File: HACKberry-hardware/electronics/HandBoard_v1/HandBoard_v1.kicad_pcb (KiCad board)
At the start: 2 copper layers, 60.8 x 54.8 mm, 10 parts, among them CON1 BARREL_JACK_MJ179PH, SW1 SW_PUSH_SKRGAQD010, SW2 SW_PUSH_SKRGAQD010, SW3 SW_PUSH_SKRGAQD010, SW4 SWITCH_SS-12SDP2, U2 3-CONDUCTOR_MINIATUIRE_JACK_M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, U3 Arduino_Micro, U5 Servo_Motor_MG90S, U6 Servo_Motor_S03N, U7 Servo_Motor_MG90S

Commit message: made the garber data of the HandBoard_v1
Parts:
- removed SW1, SW2, SW3: SW_PUSH_SKRGAQD010, HACKberry_v1:SKRGAQ0010
- removed SW4: SWITCH_SS-12SDP2, Pin_Headers:Pin_Header_Straight_1x03
- removed U7: Servo_Motor_MG90S, Pin_Headers:Pin_Header_Straight_1x03
- added SW1:MAX1: SW_PUSH_SKRGAQD010, HACKberry_v1:SKRGAQ0010, F.Cu at (101.5, 118.5)
- added SW2:MIN1: SW_PUSH_SKRGAQD010, HACKberry_v1:SKRGAQ0010, F.Cu at (113.0, 118.5)
- added SW3:Thumb1: SW_PUSH_SKRGAQD010, HACKberry_v1:SKRGAQ0010, F.Cu at (124.3, 118.5)
- added SW4:Middle1: SW_PUSH_SKRGAQD010, HACKberry_v1:SKRGAQ0010, F.Cu at (110.0, 92.5)
- added SW5: SWITCH_SS-12SDP2, Pin_Headers:Pin_Header_Straight_1x03, F.Cu at (108.8, 105.5)
- added U1: 3-CONDUCTOR_MINIATUIRE_JACK_MJ-4535-3, HACKberry_v1:MINIATURE_JACK_MJ-4535-3, F.Cu at (148.5, 125.5)
- added U4: Servo_Motor_S03N, Pin_Headers:Pin_Header_Straight_1x03, F.Cu at (119.3, 87.2)
- U2: value 3-CONDUCTOR_MINIATUIRE_JACK_MJ-4535-3 -> Arduino_Micro; footprint HACKberry_v1:MINIATURE_JACK_MJ-4535-3 -> HACKberry_v1:Arduino_Micro
- U3: value Arduino_Micro -> Seed_Studio_Adjustable_DC/DC_Power_Converter_(1.25V_-_35V/3A); footprint HACKberry_v1:Arduino_Micro -> Pin_Headers:Pin_Header_Straight_2x02
- U6: value Servo_Motor_S03N -> Servo_Motor_MG90S
- moved U2 58.9 mm to (148.5, 105.0), turned to 0 degrees
- moved CON1 55.2 mm to (115.4, 141.9)
- moved U6 52.2 mm to (112.9, 87.2), turned to 180 degrees
- moved U5 52.2 mm to (116.1, 87.2), turned to 180 degrees
- moved U3 51.5 mm to (143.3, 92.3), turned to 90 degrees
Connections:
- U3 pad 2: Net-(U3-Pad2) -> Net-(CON1-Pad3)
- U5 pad 1: Net-(U3-Pad3) -> Net-(U2-Pad5)
- U5 pad 2: Net-(U4-Pad4) -> Net-(U3-Pad4)
- U5 pad 3: Net-(U4-Pad3) -> Net-(U3-Pad3)
- U6 pad 1: Net-(U3-Pad5) -> Net-(U2-Pad6)
- U6 pad 2: Net-(U4-Pad4) -> Net-(U3-Pad4)
- U6 pad 3: Net-(U4-Pad3) -> Net-(U3-Pad3)
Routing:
- net Net-(CON1-Pad3): track 0.00 -> 137.2 mm, vias 0 -> 2
- net Net-(U2-Pad6): track 0.00 -> 72.2 mm
- net Net-(U2-Pad5): track 0.00 -> 68.1 mm
- net Net-(U2-Pad3): track 0.00 -> 60.3 mm
- net Net-(SW1:MAX1-Pad2): track 0.00 -> 60.1 mm, vias 0 -> 2
- net Net-(U3-Pad3): track 0.00 -> 50.4 mm, vias 0 -> 2
- net Net-(SW5-Pad1): track 0.00 -> 46.5 mm, vias 0 -> 2
- net Net-(SW2:MIN1-Pad2): track 0.00 -> 43.5 mm
- net Net-(SW4:Middle1-Pad2): track 0.00 -> 42.6 mm
- net Net-(U3-Pad4): track 0.00 -> 42.6 mm, vias 0 -> 2
- net Net-(CON1-Pad1): track 0.00 -> 28.8 mm
- net Net-(SW3:Thumb1-Pad2): track 0.00 -> 23.6 mm
- net Net-(U1-Pad4): track 0.00 -> 12.7 mm
- net Net-(U1-Pad2): track 0.00 -> 6.87 mm
- net Net-(U2-PadGND): track 0.00 -> 2.41 mm
- added copper zone on B.Cu, net Net-(CON1-Pad3)
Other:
- outline, holes or cut-outs redrawn
- net class Custom01 added: clearance 0.2, trace_width 1, via_dia 2, via_drill 0.4
- net class Default: trace_width 0.25 -> 0.5; via_dia 0.6 -> 1

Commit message: Updated the garber data of HandBoard_v1
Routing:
- net Net-(CON1-Pad3): track 137.2 -> 140.3 mm, vias 2 -> 3
- net Net-(U2-Pad6): track 72.2 -> 75.3 mm
- net Net-(U2-Pad5): track 68.1 -> 70.9 mm
- net Net-(SW2:MIN1-Pad2): track 43.5 -> 44.3 mm, vias 0 -> 1
- net Net-(U3-Pad4): track 42.6 -> 43.2 mm
- net Net-(SW1:MAX1-Pad2): track 60.1 -> 60.4 mm, vias 2 -> 1
- net Net-(CON1-Pad1): vias 0 -> 1
- net Net-(SW5-Pad1): vias 2 -> 1
- net Net-(SW3:Thumb1-Pad2): vias 0 -> 1
- added copper zone on F.Cu, net Net-(CON1-Pad3)
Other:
- outline, holes or cut-outs redrawn
- net class Custom01: via_drill 0.4 -> 0.5
- net class Default: via_drill 0.4 -> 0.5
- rule via_min_size: 0.4 -> 0.5

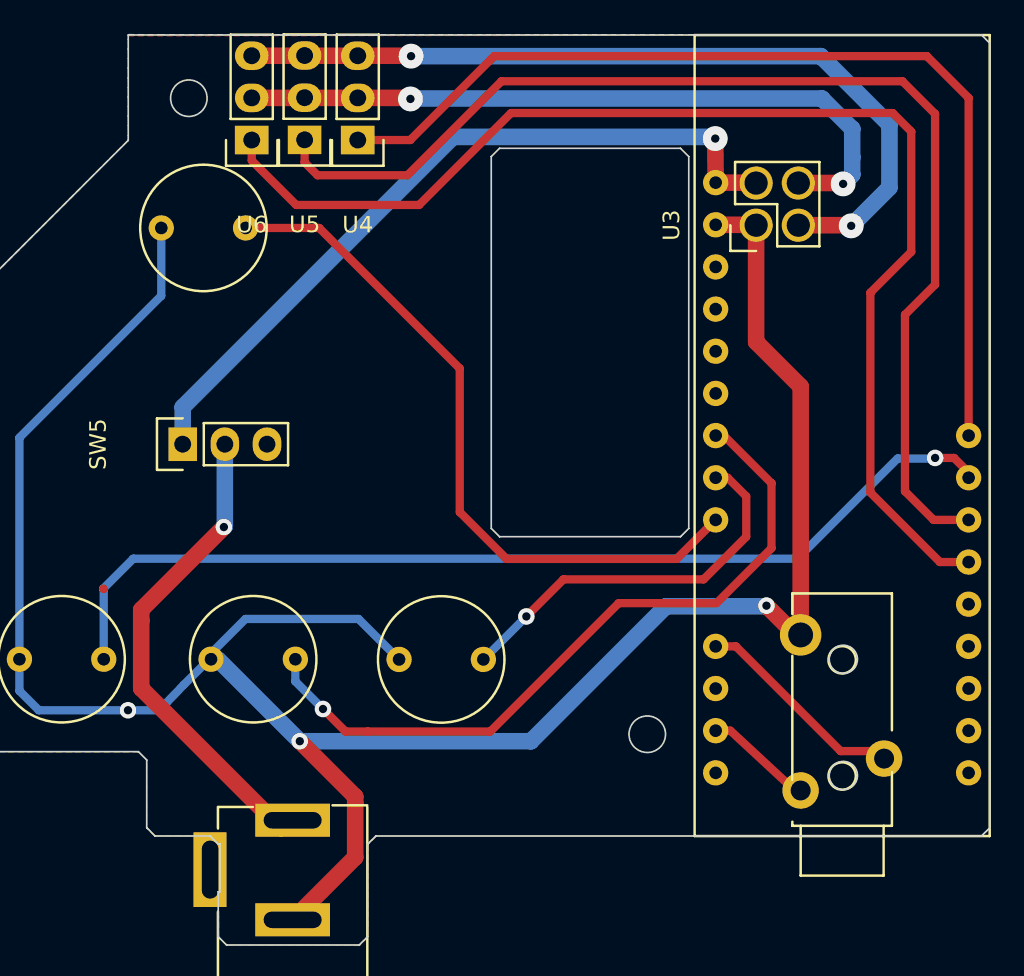
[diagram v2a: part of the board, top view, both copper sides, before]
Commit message: Fixed the error of Arduino_micro foot print
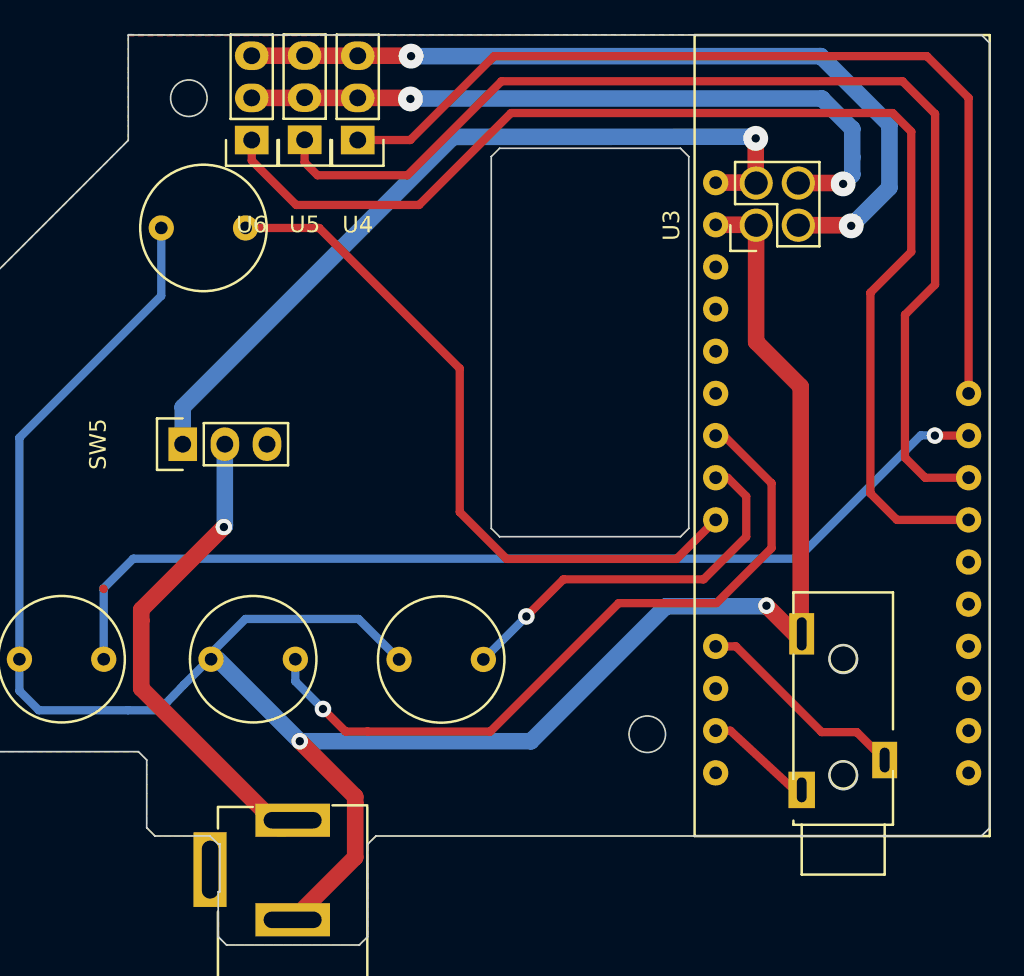
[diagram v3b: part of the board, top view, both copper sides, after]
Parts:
- moved U1 0.09 mm to (148.6, 125.5)
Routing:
- net Net-(U2-Pad3): track 60.3 -> 57.7 mm
- net Net-(SW5-Pad1): track 46.5 -> 49.0 mm
- net Net-(U2-Pad5): track 70.9 -> 68.6 mm
- net Net-(U2-Pad6): track 75.3 -> 74.2 mm
- net Net-(CON1-Pad3): vias 3 -> 2
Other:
- rule via_min_drill: 0.3 -> 0.5

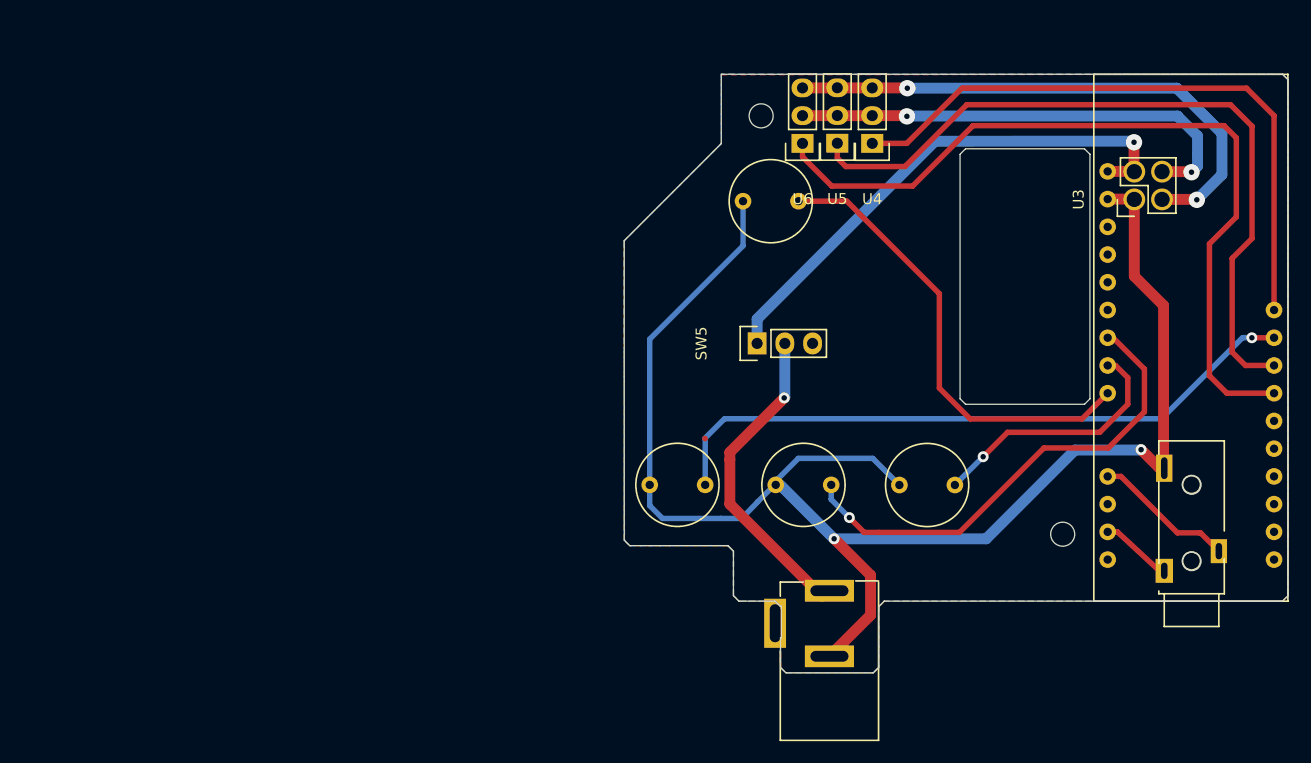
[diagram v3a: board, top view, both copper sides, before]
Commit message: Updated the HandBoard
changed the voltage for sensor from 3.3[V] to 5.0[V].
modified the garber data for milling.
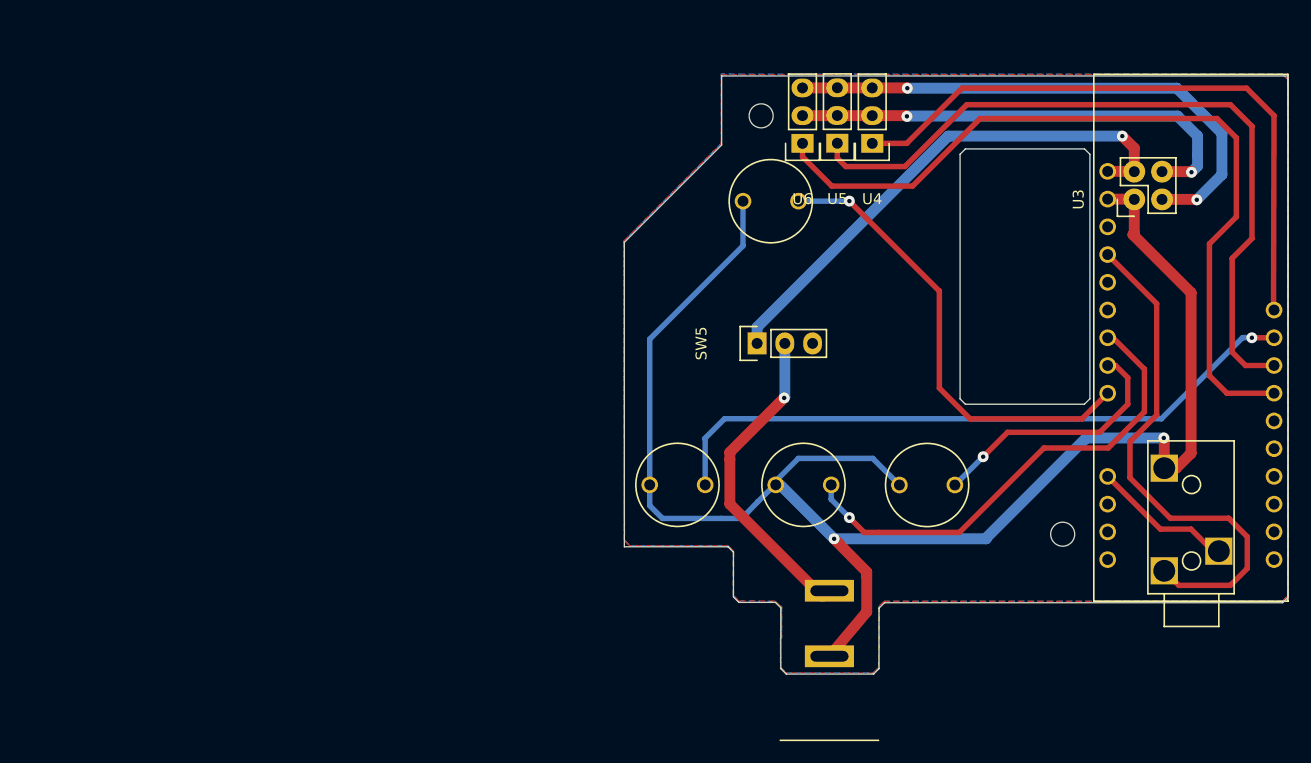
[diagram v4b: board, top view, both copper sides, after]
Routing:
- net Net-(U2-Pad5V): track 0.00 -> 46.1 mm
- net Net-(U1-Pad2): track 6.66 -> 1.89 mm
- net Net-(CON1-Pad3): track 140.3 -> 144.4 mm
- net Net-(SW5-Pad1): track 49.0 -> 48.4 mm
- net Net-(U2-Pad6): track 74.2 -> 74.8 mm
- net Net-(SW4:Middle1-Pad2): track 42.6 -> 42.8 mm, vias 0 -> 1
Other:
- outline, holes or cut-outs redrawn
- rule pad_to_mask_clearance: 0 -> 0.1
- rule via_min_drill: 0.5 -> 0.4
- rule via_min_size: 0.5 -> 0.4

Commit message: Fixed minor error
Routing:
- net Net-(U2-Pad5V): track 46.1 -> 36.3 mm
- net Net-(U1-Pad2): track 1.89 -> 11.7 mm

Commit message: Uploaded the PCB files for manufacturing
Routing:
- net Net-(U1-Pad2): track 11.7 -> 28.0 mm
- net Net-(U2-Pad5V): track 36.3 -> 20.0 mm
